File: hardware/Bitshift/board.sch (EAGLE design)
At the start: 15 parts, among them Q1 MOSFET-NCHANNELFDS6630A, U1 Tiny85-20-SMT

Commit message: added BOM, added ICSP header to board
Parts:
- added JP4: (no value), SparkFun-Connectors:M06SMD-FEMALE-V2
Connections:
- new net N$10: JP4.2, U1.PB5(NRES)
- new net N$7: JP4.6, U1.PB0(MOSI)
- net GND: now also JP4.1
- net N$4: now also JP4.3
- net N$6: now also JP4.5
- net N$9: now also JP4.4
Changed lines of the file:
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@@
 <part name="R6" library="SparkFun-Resistors" deviceset="RESISTOR" device="0805-RES"/>
 <part name="R4" library="SparkFun-Resistors" deviceset="RESISTOR" device="0603"/>
+<part name="GND6" library="supply1" deviceset="GND" device=""/>
+<part name="JP4" library="SparkFun-Connectors" deviceset="M06" device="SMD-FEMALE-V2"/>
 </parts>
 <sheets>
@@
 <instance part="R6" gate="G$1" x="91.44" y="55.88" rot="R90"/>
 <instance part="R4" gate="G$1" x="-7.62" y="101.6" rot="R90"/>
+<instance part="GND6" gate="1" x="88.9" y="119.38" rot="R270"/>
+<instance part="JP4" gate="G$1" x="109.22" y="111.76" rot="R180"/>
 </instances>
 <busses>
@@
 <junction x="165.1" y="78.74"/>
 </segment>
+<segment>
+<pinref part="GND6" gate="1" pin="GND"/>
+<pinref part="JP4" gate="G$1" pin="1"/>
+<wire x1="91.44" y1="119.38" x2="104.14" y2="119.38" width="0.1524" layer="91"/>
+<wire x1="104.14" y1="119.38" x2="104.14" y2="116.84" width="0.1524" layer="91"/>
+</segment>
 </net>
 <net name="VCC" class="0">
@@
 <wire x1="33.02" y1="78.74" x2="33.02" y2="81.28" width="0.1524" layer="91"/>
 <junction x="33.02" y="81.28"/>
+<pinref part="JP4" gate="G$1" pin="3"/>
+<wire x1="104.14" y1="111.76" x2="43.18" y2="111.76" width="0.1524" layer="91"/>
+<wire x1="43.18" y1="111.76" x2="43.18" y2="81.28" width="0.1524" layer="91"/>
 </segment>
 </net>
@@
 <pinref part="U1" gate="G$1" pin="PB1(MISO)"/>
 <pinref part="R1" gate="G$1" pin="2"/>
-<wire x1="76.2" y1="78.74" x2="139.7" y2="78.74" width="0.1524" layer="91"/>
+<wire x1="76.2" y1="78.74" x2="91.44" y2="78.74" width="0.1524" layer="91"/>
+<wire x1="91.44" y1="78.74" x2="139.7" y2="78.74" width="0.1524" layer="91"/>
 <wire x1="139.7" y1="78.74" x2="139.7" y2="71.12" width="0.1524" layer="91"/>
 <wire x1="139.7" y1="78.74" x2="142.24" y2="78.74" width="0.1524" layer="91"/>
@@
 <pinref part="JP2" gate="G$1" pin="3"/>
 <wire x1="142.24" y1="73.66" x2="165.1" y2="73.66" width="0.1524" layer="91"/>
+<pinref part="JP4" gate="G$1" pin="5"/>
+<wire x1="104.14" y1="106.68" x2="91.44" y2="106.68" width="0.1524" layer="91"/>
+<wire x1="91.44" y1="106.68" x2="91.44" y2="78.74" width="0.1524" layer="91"/>
+<junction x="91.44" y="78.74"/>
 </segment>
 </net>
@@
 <wire x1="83.82" y1="76.2" x2="83.82" y2="71.12" width="0.1524" layer="91"/>
 <junction x="83.82" y="76.2"/>
-</segment>
-</net>
+<pinref part="JP4" gate="G$1" pin="4"/>
+<wire x1="104.14" y1="109.22" x2="83.82" y2="109.22" width="0.1524" layer="91"/>
+<wire x1="83.82" y1="109.22" x2="83.82" y2="76.2" width="0.1524" layer="91"/>
+</segment>
+</net>
+<net name="N$10" class="0">
+<segment>
+<pinref part="U1" gate="G$1" pin="PB5(NRES)"/>
+<wire x1="81.28" y1="68.58" x2="76.2" y2="68.58" width="0.1524" layer="91"/>
+<pinref part="JP4" gate="G$1" pin="2"/>
+<wire x1="104.14" y1="114.3" x2="81.28" y2="114.3" width="0.1524" layer="91"/>
+<wire x1="81.28" y1="114.3" x2="81.28" y2="68.58" width="0.1524" layer="91"/>
+</segment>
+</net>
+<net name="N$7" class="0">
+<segment>
+<pinref part="JP4" gate="G$1" pin="6"/>
+<pinref part="U1" gate="G$1" pin="PB0(MOSI)"/>
+<wire x1="104.14" y1="104.14" x2="76.2" y2="104.14" width="0.1524" layer="91"/>
+<wire x1="76.2" y1="104.14" x2="76.2" y2="81.28" width="0.1524" layer="91"/>
+</segment>
+</net>

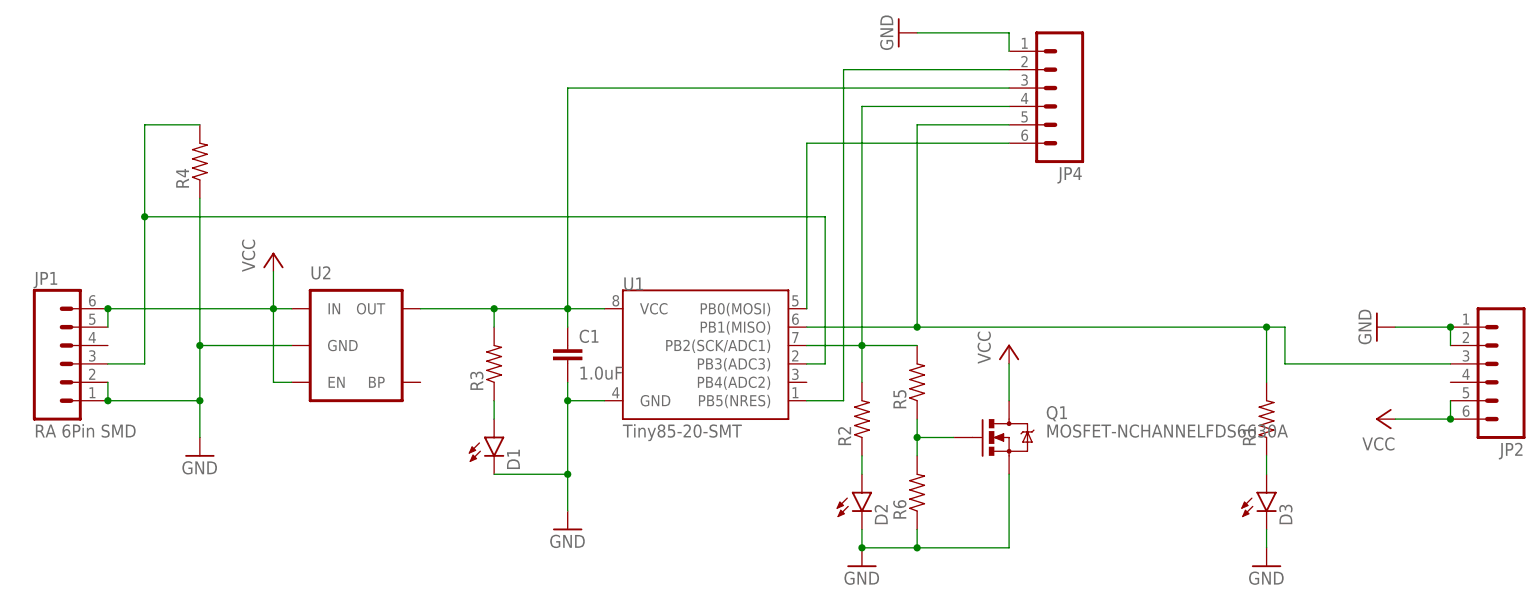
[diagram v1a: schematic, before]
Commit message: added decoupling cap for voltage regulator in BOM
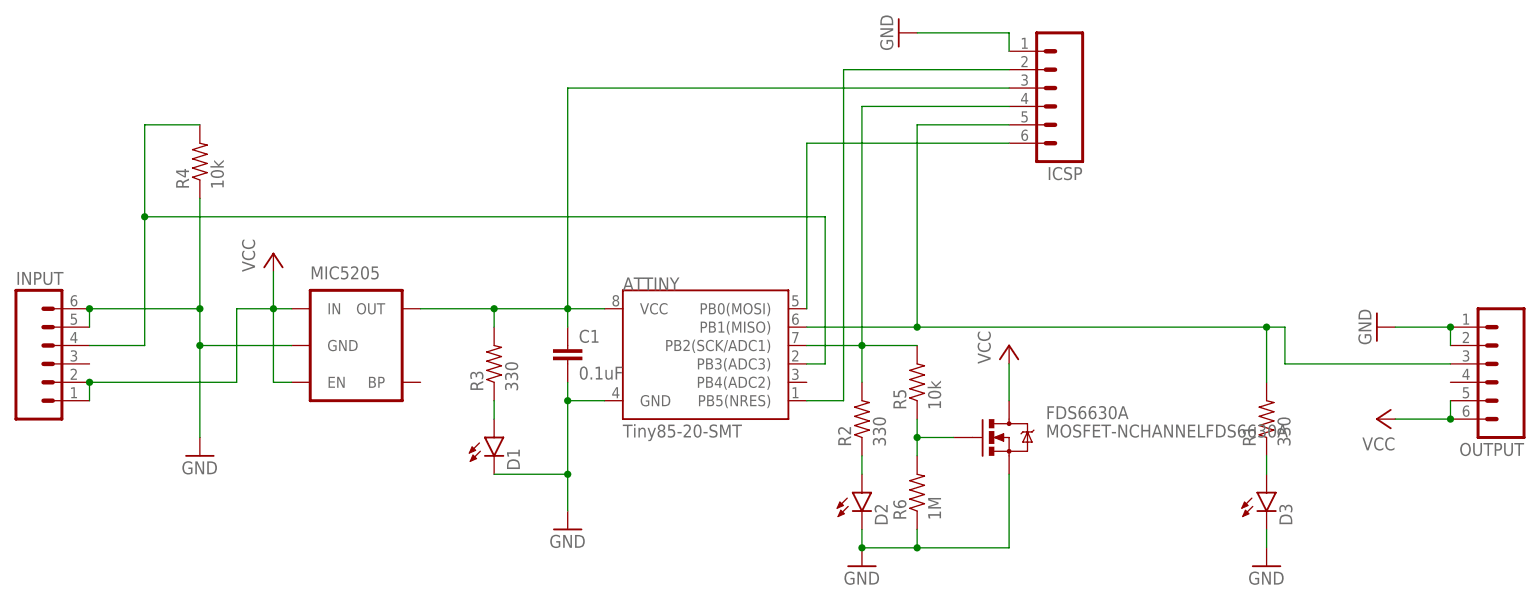
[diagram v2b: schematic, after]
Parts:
- removed JP1: RA 6Pin SMD, SparkFun-Connectors:M06SMD
- added INPUT: (no value), SparkFun-Connectors:M06SMD-FEMALE-V2
- C1: value 1.0uF -> 0.1uF
- R1, R2, R3: value (none) -> 330
- R4, R5: value (none) -> 10k
- R6: value (none) -> 1M
- renumbered JP2 to OUTPUT, JP4 to ICSP, Q1 to FDS6630A, U1 to ATTINY, U2 to MIC5205
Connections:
- net GND: now also INPUT.5, INPUT.6; no longer JP1.1, JP1.2
- net N$5: now also INPUT.4; no longer JP1.3
- net VCC: now also INPUT.1, INPUT.2; no longer JP1.5, JP1.6

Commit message: moved things around
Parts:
- added C2: 0.1uF, SparkFun-Capacitors:1.0UF-25V-+80/-20(0805)
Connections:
- net GND: now also C2.2
- net N$4: now also C2.1
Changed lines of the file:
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@@
 <part name="ICSP" library="SparkFun-Connectors" deviceset="M06" device="SMD-FEMALE-V2"/>
 <part name="INPUT" library="SparkFun-Connectors" deviceset="M06" device="SMD-FEMALE-V2"/>
+<part name="C2" library="SparkFun-Capacitors" deviceset="1.0UF-25V-+80/-20(0805)" device="" value="0.1uF"/>
 </parts>
 <sheets>
@@
 <instance part="ICSP" gate="G$1" x="109.22" y="111.76" rot="R180"/>
 <instance part="INPUT" gate="G$1" x="-27.94" y="73.66"/>
+<instance part="C2" gate="G$1" x="15.24" y="60.96" rot="R270"/>
 </instances>
 <busses>
@@
 <pinref part="MIC5205" gate="G$1" pin="GND"/>
 <pinref part="GND5" gate="1" pin="GND"/>
-<wire x1="5.08" y1="76.2" x2="-7.62" y2="76.2" width="0.1524" layer="91"/>
+<wire x1="5.08" y1="76.2" x2="0" y2="76.2" width="0.1524" layer="91"/>
+<wire x1="0" y1="76.2" x2="-7.62" y2="76.2" width="0.1524" layer="91"/>
 <wire x1="-7.62" y1="76.2" x2="-7.62" y2="63.5" width="0.1524" layer="91"/>
 <pinref part="R4" gate="G$1" pin="1"/>
@@
 <wire x1="-22.86" y1="81.28" x2="-22.86" y2="78.74" width="0.1524" layer="91"/>
 <junction x="-22.86" y="81.28"/>
+<pinref part="C2" gate="G$1" pin="2"/>
+<wire x1="12.7" y1="60.96" x2="0" y2="60.96" width="0.1524" layer="91"/>
+<wire x1="0" y1="60.96" x2="0" y2="76.2" width="0.1524" layer="91"/>
+<junction x="0" y="76.2"/>
 </segment>
 <segment>
@@
 <pinref part="MIC5205" gate="G$1" pin="OUT"/>
 <pinref part="ATTINY" gate="G$1" pin="VCC"/>
-<wire x1="22.86" y1="81.28" x2="33.02" y2="81.28" width="0.1524" layer="91"/>
+<wire x1="22.86" y1="81.28" x2="25.4" y2="81.28" width="0.1524" layer="91"/>
 <pinref part="C1" gate="G$1" pin="1"/>
+<wire x1="25.4" y1="81.28" x2="33.02" y2="81.28" width="0.1524" layer="91"/>
 <wire x1="33.02" y1="81.28" x2="43.18" y2="81.28" width="0.1524" layer="91"/>
 <wire x1="43.18" y1="81.28" x2="48.26" y2="81.28" width="0.1524" layer="91"/>
@@
 <wire x1="104.14" y1="111.76" x2="43.18" y2="111.76" width="0.1524" layer="91"/>
 <wire x1="43.18" y1="111.76" x2="43.18" y2="81.28" width="0.1524" layer="91"/>
+<pinref part="C2" gate="G$1" pin="1"/>
+<wire x1="20.32" y1="60.96" x2="25.4" y2="60.96" width="0.1524" layer="91"/>
+<wire x1="25.4" y1="60.96" x2="25.4" y2="81.28" width="0.1524" layer="91"/>
+<junction x="25.4" y="81.28"/>
 </segment>
 </net>
@@
 </sheet>
 </sheets>
+<errors>
+</errors>
 </schematic>
 </drawing>
